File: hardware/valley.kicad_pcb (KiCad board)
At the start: 2 copper layers, 28 parts, among them IC1 ATMEGA1284P-A, P1 CONN_01X10, P2 USB_OTG, P3 CONN_02X03, P4 CONN_01X16, Q1 BSS138, Q2 BSS138, U1 CH340G, U2 AP111733, U3 TXS0108E, Y1 12M

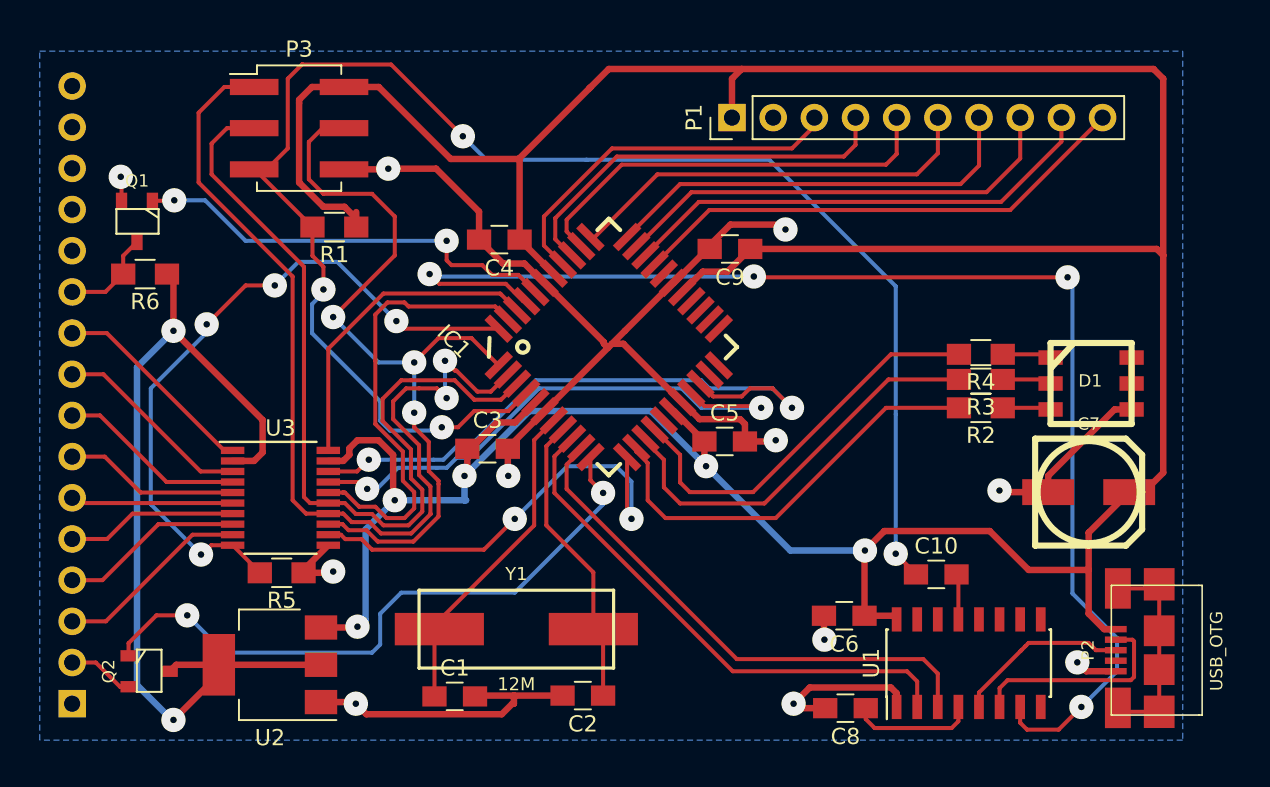
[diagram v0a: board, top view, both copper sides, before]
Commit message: Moving LED to back of board.
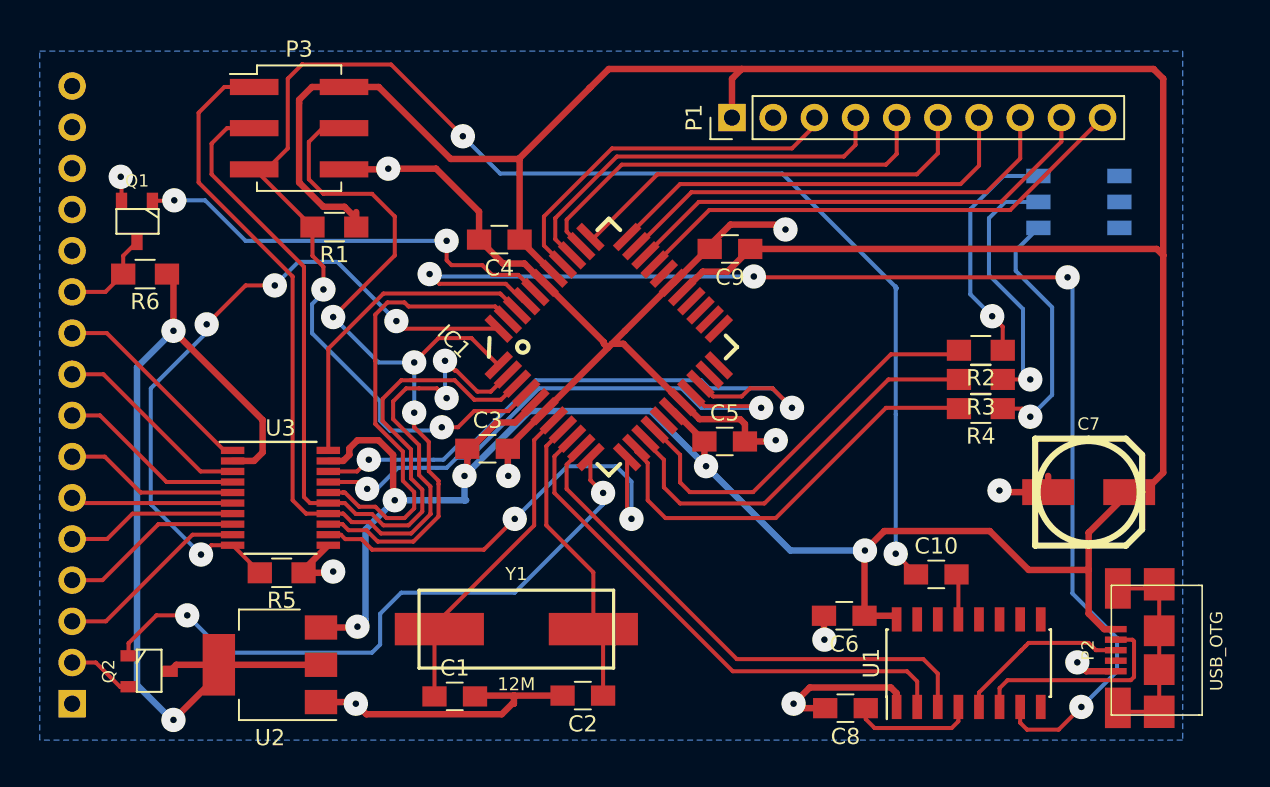
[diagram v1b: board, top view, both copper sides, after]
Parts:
- D1: moved to B.Cu
- moved D1 11.2 mm to (183.6, 47.3)
- moved R2 3.55 mm to (177.6, 56.5)
- moved R4 3.35 mm to (177.6, 60.0)
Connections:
- IC1 pad 13: LED_BLUE -> LED_RED
- IC1 pad 15: LED_RED -> LED_BLUE
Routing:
- net Net-(D1-Pad5): track 3.05 -> 16.2 mm, vias 0 -> 1
- net Net-(D1-Pad6): track 3.03 -> 15.6 mm, vias 0 -> 1
- net Net-(D1-Pad4): track 2.99 -> 14.6 mm, vias 0 -> 1
- net GND: track 112.1 -> 102.1 mm
- net LED_RED: track 24.9 -> 26.0 mm
- net LED_BLUE: track 26.0 -> 24.9 mm

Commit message: Updating schematic to link SDA/MOSI and SCL/SCK.
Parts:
- removed Q1: BSS138, cbrues/kicad-lib2/footprints/sm-ics.pretty:SM-SOT23
- moved C2 3.56 mm to (153.2, 74.2)
- moved C1 3.51 mm to (145.3, 74.3)
- moved Y1 2.91 mm to (149.1, 70.8)
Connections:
- IC1 pad 19: SCL -> Net-(IC1-Pad19)
- IC1 pad 20: SDA -> Net-(IC1-Pad20)
- P4 pad 15: Net-(P4-Pad15) -> +3V3
- P4 pad 16: Net-(P4-Pad16) -> GND
- P4 pad 8: Net-(P4-Pad8) -> Net-(P4-Pad6)
- P4 pad 9: Net-(P4-Pad9) -> Net-(P4-Pad4)
- U3 pad 1: Net-(P4-Pad10) -> Net-(P4-Pad11)
- U3 pad 17: SCL -> A0
- U3 pad 18: SDA -> Net-(U3-Pad18)
- U3 pad 20: A0 -> RESET_TFT
- U3 pad 3: Net-(P4-Pad9) -> Net-(U3-Pad3)
- U3 pad 4: Net-(P4-Pad8) -> Net-(P4-Pad10)
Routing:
- net SDA: track 38.3 -> 0.00 mm, vias 2 -> 0
- net SCL: track 34.6 -> 0.00 mm, vias 2 -> 0
- net BACKLIGHT: track 39.9 -> 65.0 mm
- net CS_SD: track 27.8 -> 49.0 mm
- net Net-(P4-Pad4): track 11.3 -> 26.7 mm, vias 0 -> 2
- net Net-(P4-Pad9): track 12.4 -> 0.00 mm
- net GND: track 102.1 -> 89.8 mm
- net Net-(P4-Pad11): track 5.94 -> 17.8 mm
- net +3V3: track 55.5 -> 67.2 mm
- net Net-(P4-Pad8): track 11.6 -> 0.00 mm
- net Net-(P4-Pad6): track 10.0 -> 18.6 mm, vias 0 -> 2
- net RESET_TFT: track 26.7 -> 33.4 mm
- net A0: track 19.8 -> 23.9 mm, vias 0 -> 2
- net Net-(C1-Pad1): track 20.1 -> 16.5 mm
- net Net-(C2-Pad1): track 18.3 -> 14.8 mm
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
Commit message: Removing some unnecessary pullup resistors.
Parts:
- removed R5, R6: 10k, Resistors_SMD:R_0805_HandSoldering
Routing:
- net Net-(P4-Pad11): track 17.8 -> 15.2 mm
- net GND: track 89.8 -> 87.4 mm
- net ENABLE_LC: track 40.7 -> 38.4 mm

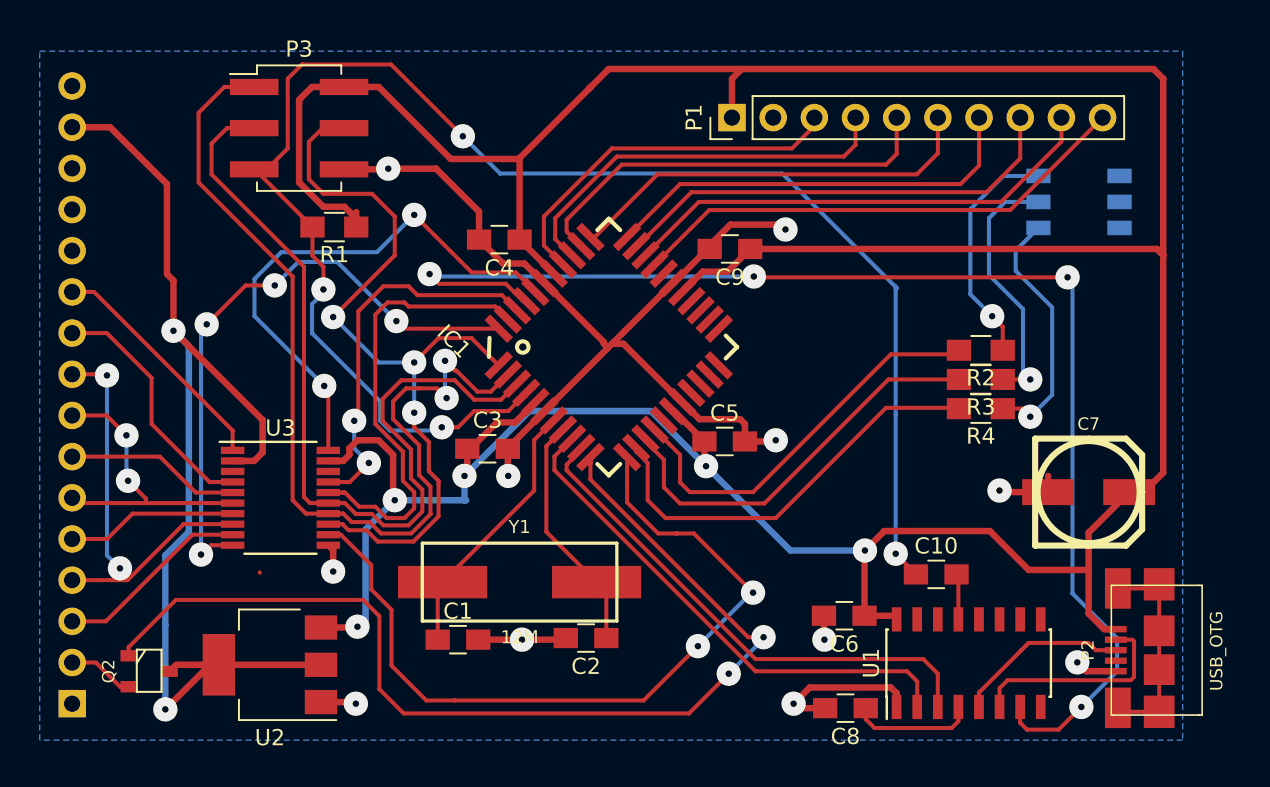
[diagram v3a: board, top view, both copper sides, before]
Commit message: Updating schematics for wider trace width; 15mil is enough.
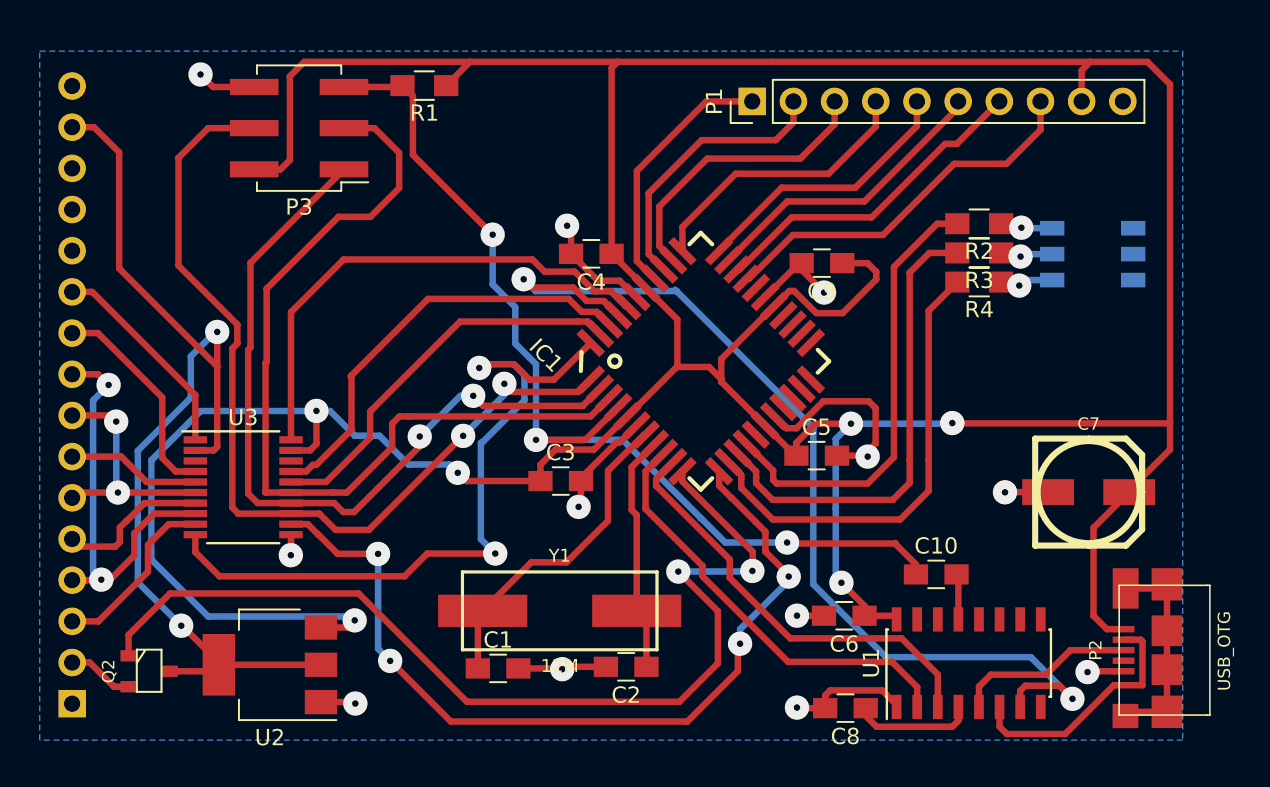
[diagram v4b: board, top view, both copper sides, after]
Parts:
- moved R1 10.3 mm to (143.2, 40.1)
- moved R2 7.81 mm to (177.4, 48.6)
- moved R3 7.81 mm to (177.4, 50.4)
- moved R4 7.81 mm to (177.4, 52.2)
- moved C4 5.74 mm to (153.5, 50.5)
- moved C5 5.74 mm to (167.4, 63.0)
- moved C9 5.74 mm to (167.8, 51.1)
- moved IC1 5.74 mm to (160.3, 57.1)
- moved C3 4.93 mm to (151.6, 64.5)
- moved D1 3.33 mm to (184.4, 50.5)
- moved C2 3.05 mm to (155.7, 76.0)
- moved C1 3.05 mm to (147.8, 76.1)
- moved Y1 3.05 mm to (151.6, 72.5)
- moved U3 2.39 mm to (132.1, 64.9)
- moved P1 1.60 mm to (163.4, 41.1)
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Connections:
- P1 pad 1: +5V -> Net-(IC1-Pad37)
- P1 pad 10: Net-(IC1-Pad30) -> GND
- P1 pad 2: GND -> Net-(IC1-Pad36)
- P1 pad 3: Net-(IC1-Pad37) -> Net-(IC1-Pad35)
- P1 pad 4: Net-(IC1-Pad36) -> Net-(IC1-Pad34)
- P1 pad 5: Net-(IC1-Pad35) -> Net-(IC1-Pad33)
- P1 pad 6: Net-(IC1-Pad34) -> Net-(IC1-Pad32)
- P1 pad 7: Net-(IC1-Pad33) -> Net-(IC1-Pad31)
- P1 pad 8: Net-(IC1-Pad32) -> Net-(IC1-Pad30)
- P1 pad 9: Net-(IC1-Pad31) -> +5V
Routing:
- net RESET: track 98.5 -> 62.1 mm, vias 4 -> 3
- net GND: track 87.4 -> 57.9 mm, vias 11 -> 12
- net +5V: track 236.6 -> 256.1 mm, vias 5 -> 6
- net CLKO: track 80.3 -> 61.8 mm, vias 4 -> 2
- net Net-(D1-Pad5): track 16.2 -> 3.31 mm
- net Net-(D1-Pad6): track 15.6 -> 3.38 mm
- net Net-(D1-Pad4): track 14.6 -> 3.26 mm
- net MISO: track 59.5 -> 48.6 mm
- net Net-(IC1-Pad32): track 28.4 -> 18.5 mm
- net Net-(IC1-Pad31): track 30.0 -> 20.5 mm
- net Net-(IC1-Pad33): track 26.5 -> 17.0 mm
- net Net-(IC1-Pad35): track 26.3 -> 18.0 mm
- net Net-(IC1-Pad34): track 25.8 -> 17.8 mm
- net Net-(IC1-Pad30): track 31.4 -> 23.7 mm
- net Net-(IC1-Pad36): track 24.8 -> 17.2 mm
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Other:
- net class Default: trace_width 0.25 -> 0.4

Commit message: Updating schematic for v 1.1.
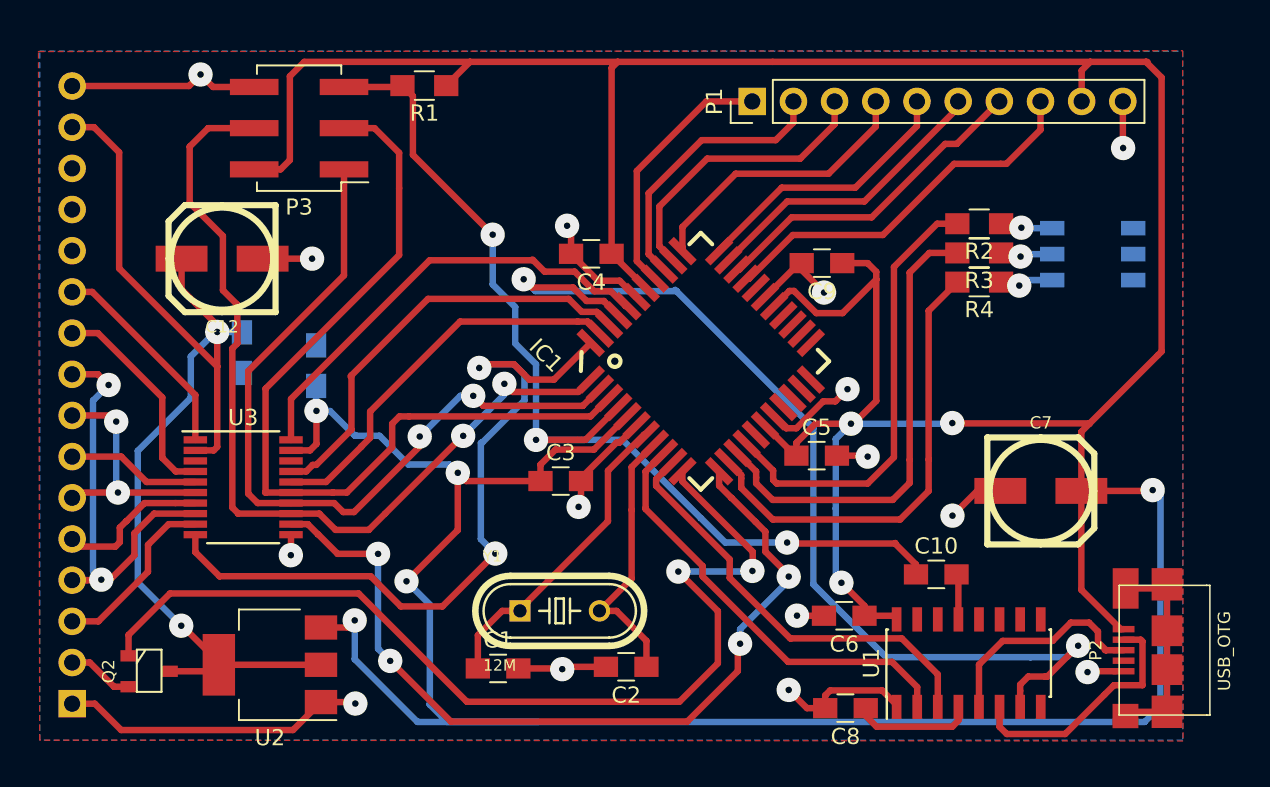
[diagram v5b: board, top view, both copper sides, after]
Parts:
- added C11: 0.1u, Capacitors_SMD:C_0805_HandSoldering, B.Cu at (136.6, 57.4)
- added C12: 47u, cbrues/kicad-lib2/footprints/capacitors.pretty:SMD_PANASONIC_D, F.Cu at (130.8, 50.8)
- added C13: 0.1u, Capacitors_SMD:C_0805_HandSoldering, B.Cu at (132.0, 56.6)
- Y1: footprint tmk/keyboard_parts.pretty:HC-49_SMT -> monostable/CommonPartsLibrary.pretty:XTAL_HC-49US-16.000MHZ
- moved C7 2.95 mm to (181.2, 65.1)
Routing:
- net +5V: track 256.1 -> 303.6 mm, vias 6 -> 8
- net GND: track 57.9 -> 86.2 mm, vias 12 -> 15
- net +3V3: track 62.0 -> 69.2 mm
- net Net-(P2-Pad3): track 10.6 -> 13.8 mm
- net RESET_TFT: track 31.2 -> 28.1 mm
- net Net-(C2-Pad1): track 14.7 -> 17.0 mm
- net ENABLE_LC: track 44.8 -> 46.3 mm
- net SCK: track 54.0 -> 52.9 mm
- net CLKO: track 61.8 -> 62.6 mm
- net Net-(C1-Pad1): track 20.0 -> 19.4 mm
- net MOSI: track 56.0 -> 55.4 mm
- added copper zone on F.Cu, net (none)
